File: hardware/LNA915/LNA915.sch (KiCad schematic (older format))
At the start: 25 parts, among them P1 SMA-KIT-1.5MF, U1 SWITCH, U2 SAW, U3 LNA, U4 SWITCH

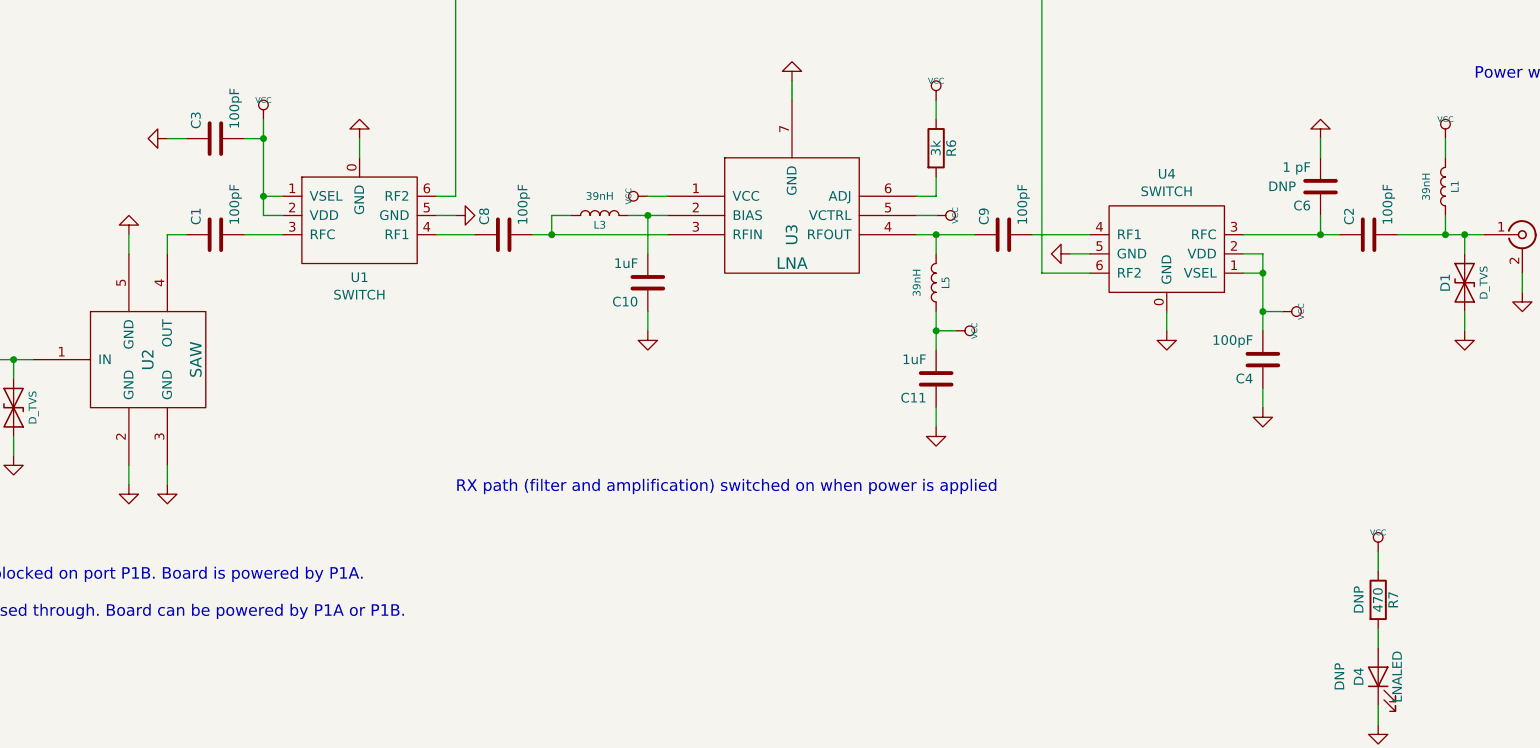
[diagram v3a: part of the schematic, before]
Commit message: LNA915: renumber reference designators
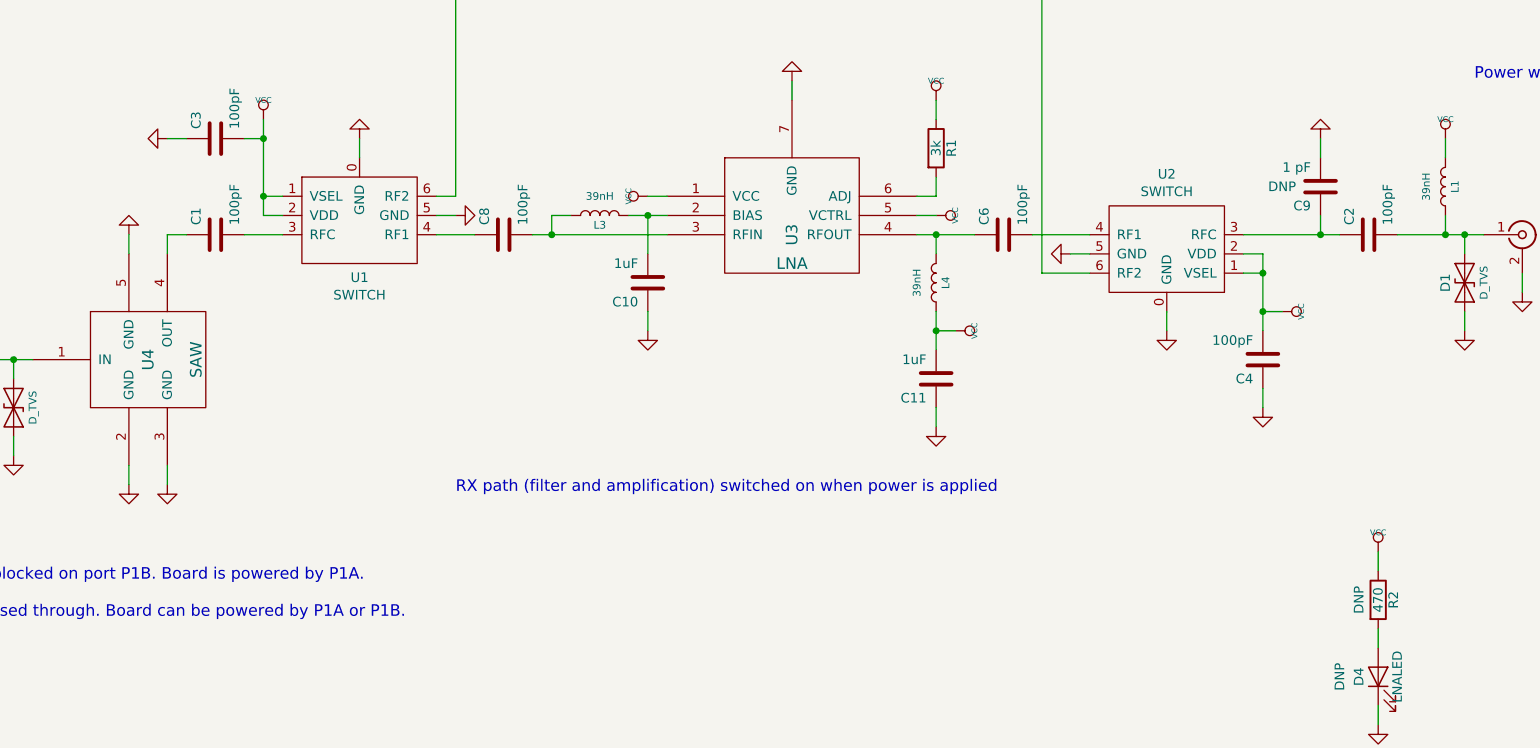
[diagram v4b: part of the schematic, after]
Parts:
- renumbered C9 to C6, C6 to C9, L5 to L4, R6 to R1, R7 to R2, U4 to U2, U2 to U4
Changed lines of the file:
@@
 Connection ~ 2200 3900
 $Comp
-L hackrf:FAR-F5QA U2
+L hackrf:FAR-F5QA U4
 U 1 1 52F44412
 P 2900 3900
-F 0 "U2" V 2900 3900 60  0000 C CNN
+F 0 "U4" V 2900 3900 60  0000 C CNN
 F 1 "SAW" V 3150 3900 60  0000 C CNN
 F 2 "LNA915:F5Q" H 2900 3900 60  0001 C CNN
@@
 	5500 3050 5600 3050
 $Comp
-L Device:R R6
+L Device:R R1
 U 1 1 52F68800
 P 7000 2800
-F 0 "R6" V 7080 2800 50  0000 C CNN
+F 0 "R1" V 7080 2800 50  0000 C CNN
 F 1 "3k" V 7000 2800 50  0000 C CNN
 F 2 "gsg-modules:0402" H 7000 2800 50  0001 C CNN
@@
 Connection ~ 5000 3250
 $Comp
-L Device:L L5
+L Device:L L4
 U 1 1 52F688CD
 P 7000 3500
-F 0 "L5" V 6950 3500 40  0000 C CNN
+F 0 "L4" V 6950 3500 40  0000 C CNN
 F 1 "39nH" V 7100 3500 40  0000 C CNN
 F 2 "gsg-modules:0402" H 7000 3500 50  0001 C CNN
@@
 $EndComp
 $Comp
-L Device:R R7
+L Device:R R2
 U 1 1 52F68CBB
 P 9300 5150
-F 0 "R7" V 9380 5150 50  0000 C CNN
+F 0 "R2" V 9380 5150 50  0000 C CNN
 F 1 "470" V 9300 5150 50  0000 C CNN
 F 2 "gsg-modules:0402" H 9300 5150 50  0001 C CNN
@@
 $EndComp
 $Comp
-L Device:C C9
+L Device:C C6
 U 1 1 52F69EBA
 P 7350 3250
-F 0 "C9" H 7400 3350 50  0000 L CNN
+F 0 "C6" H 7400 3350 50  0000 L CNN
 F 1 "100pF" H 7400 3150 50  0000 L CNN
 F 2 "gsg-modules:0402" H 7350 3250 50  0001 C CNN
@@
 	4400 3250 4600 3250
 $Comp
-L LNA915:GRF6011 U4
+L LNA915:GRF6011 U2
 U 1 1 5EF6E285
 P 8200 3350
-F 0 "U4" H 8200 2935 50  0000 C CNN
+F 0 "U2" H 8200 2935 50  0000 C CNN
 F 1 "SWITCH" H 8200 3026 50  0000 C CNN
 F 2 "LNA915:GRF6011" H 8200 3350 50  0001 C CNN
@@
 $EndComp
 $Comp
-L Device:C C6
+L Device:C C9
 U 1 1 5F2886C8
 P 9000 3000
-F 0 "C6" H 9050 3100 50  0000 L CNN
+F 0 "C9" H 9050 3100 50  0000 L CNN
 F 1 "1 pF" H 9050 2900 50  0000 L CNN
 F 2 "gsg-modules:0402" H 9000 3000 50  0001 C CNN

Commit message: LNA915: use gsg-kicad-lib instead of hackrf library
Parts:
- U3: symbol hackrf:BGB741L7ESD -> gsg-symbols:BGB741L7ESD
- U4: symbol hackrf:FAR-F5QA -> gsg-symbols:FAR-F5QA
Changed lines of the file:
@@
 Connection ~ 2200 3900
 $Comp
-L hackrf:FAR-F5QA U4
+L gsg-symbols:FAR-F5QA U4
 U 1 1 52F44412
 P 2900 3900
@@
 $EndComp
 $Comp
-L hackrf:BGB741L7ESD U3
+L gsg-symbols:BGB741L7ESD U3
 U 1 1 52F68792
 P 6250 3150
